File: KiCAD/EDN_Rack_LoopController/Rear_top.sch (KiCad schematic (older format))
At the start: 153 parts, among them J1 AudioJack2_Switch, J10 SW CTRL1, J11 AudioJack2_Switch, J12 AudioJack2_Switch, J13 AudioJack2_Switch, J14 AudioJack2_Switch, J2 AudioJack2_Switch, J3 AudioJack2_Switch, J4 AudioJack2_Switch, J9 To Preamp In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

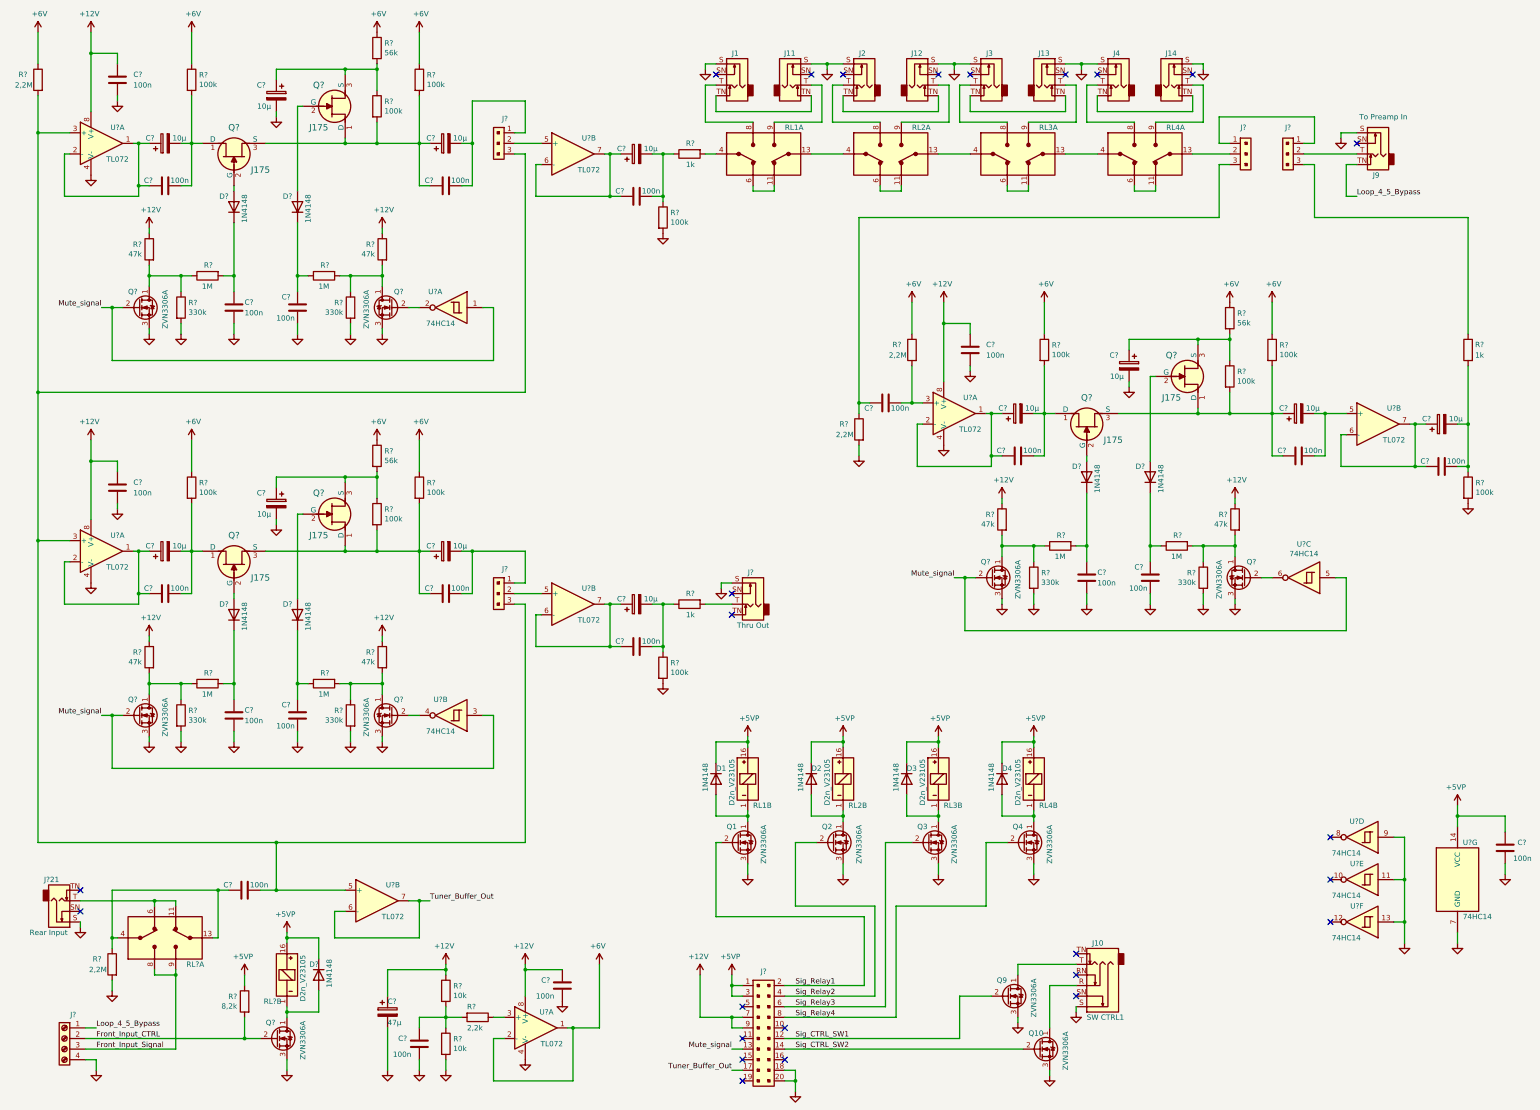
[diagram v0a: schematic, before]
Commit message: Schematic polish, added complete schematic pdf.
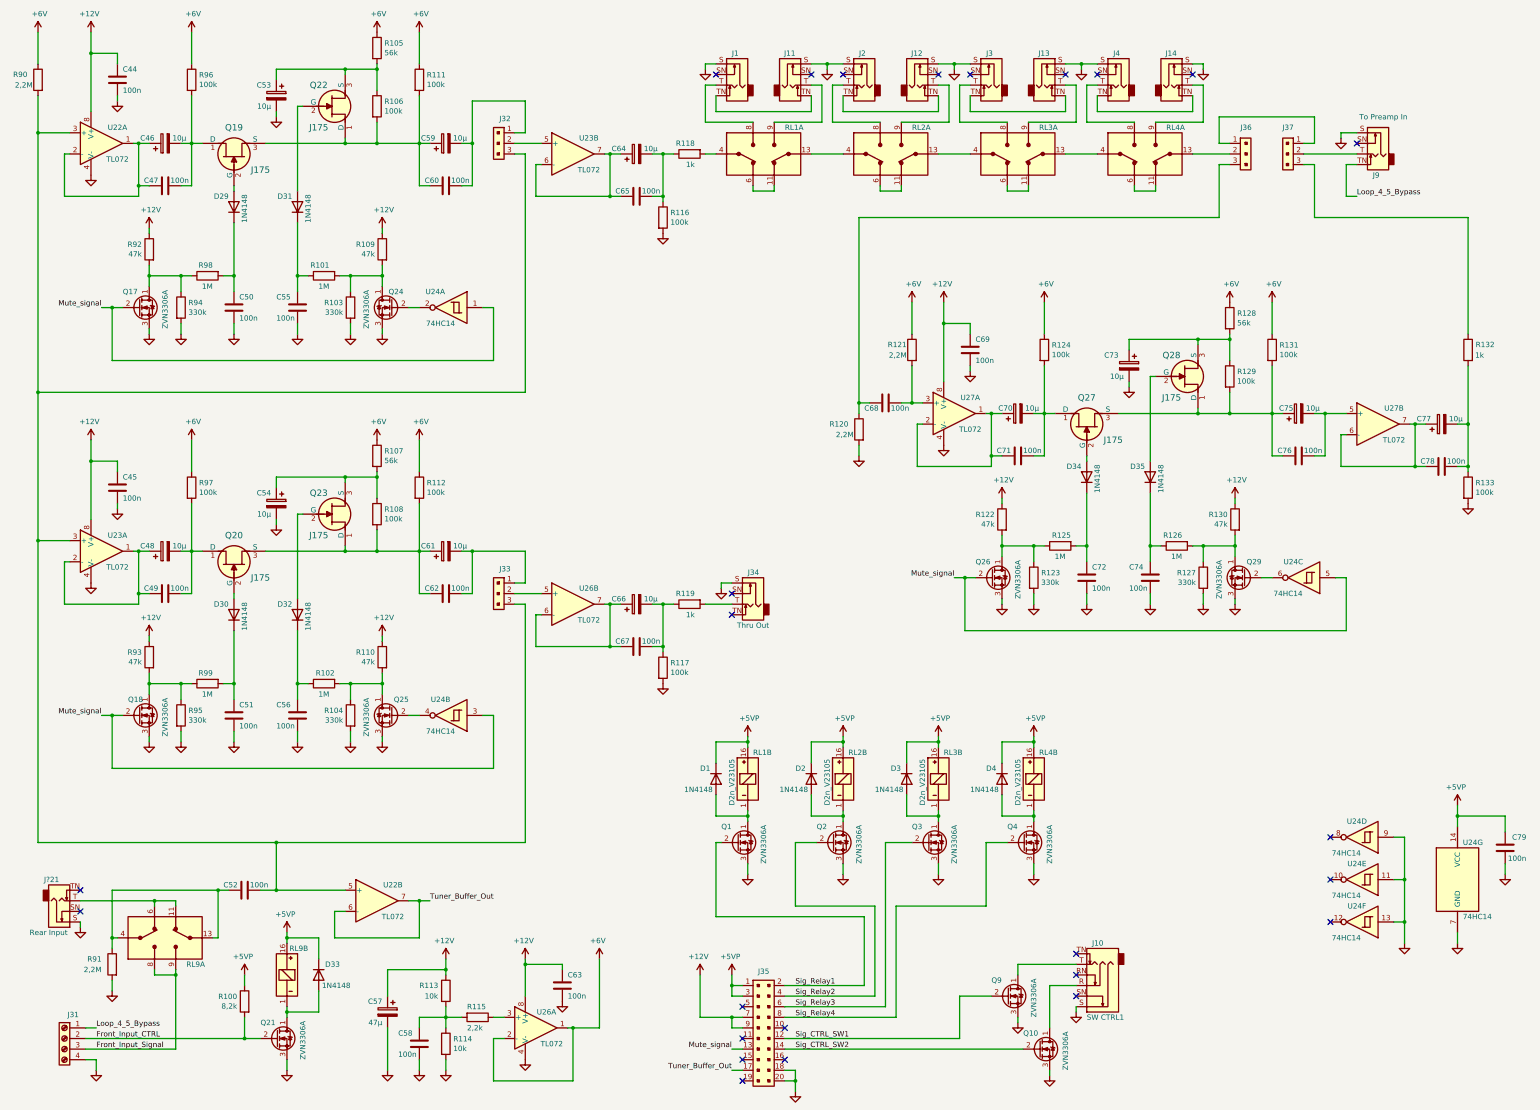
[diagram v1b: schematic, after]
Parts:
- gave numbers to parts that had none: 114
